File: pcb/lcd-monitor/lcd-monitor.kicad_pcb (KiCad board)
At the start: 2 copper layers, 50 parts, among them J1 Conn_01x07_Male, J2 Conn_01x08_Male, J3 Conn_02x05_Odd_Even, J4 Screw_Terminal_01x02, J5 Conn_01x06_Male, SW1 SW_Push, U1 PC817, U10 AZ1117-3.3, U2 PC817, U3 PC817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

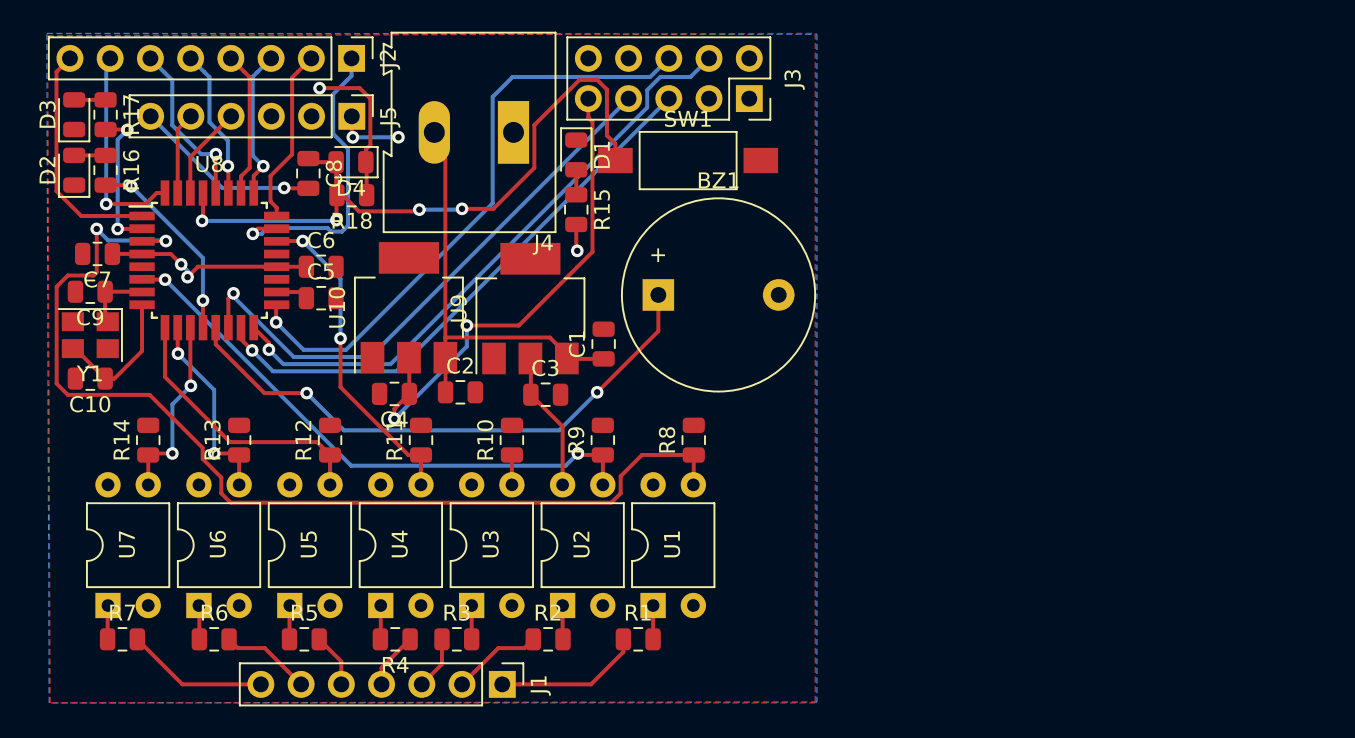
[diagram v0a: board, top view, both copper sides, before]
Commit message: Add zone status led
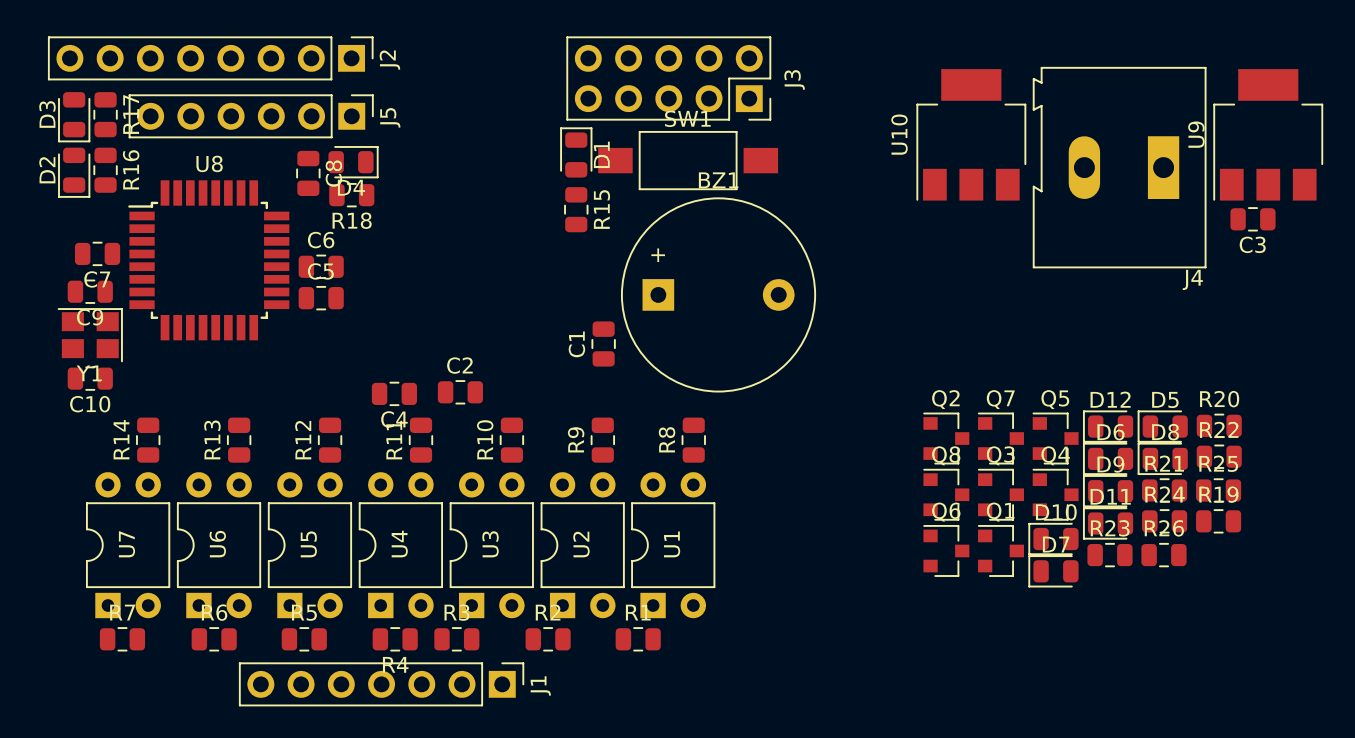
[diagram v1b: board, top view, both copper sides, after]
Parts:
- added D10: LED, LED_SMD:LED_0805_2012Metric, F.Cu at (205.2, 85.7)
- added D11: LED, LED_SMD:LED_0805_2012Metric, F.Cu at (208.7, 84.7)
- added D12: D, Diode_SMD:D_0805_2012Metric, F.Cu at (208.7, 78.6)
- added D5: LED, LED_SMD:LED_0805_2012Metric, F.Cu at (212.1, 78.6)
- added D6: LED, LED_SMD:LED_0805_2012Metric, F.Cu at (208.7, 80.7)
- added D7: LED, LED_SMD:LED_0805_2012Metric, F.Cu at (205.2, 87.8)
- added D8: LED, LED_SMD:LED_0805_2012Metric, F.Cu at (212.1, 80.7)
- added D9: LED, LED_SMD:LED_0805_2012Metric, F.Cu at (208.7, 82.7)
- added Q1: 2N7002, Package_TO_SOT_SMD:SOT-23, F.Cu at (201.8, 86.5)
- added Q2: 2N7002, Package_TO_SOT_SMD:SOT-23, F.Cu at (198.3, 79.4)
- added Q3: 2N7002, Package_TO_SOT_SMD:SOT-23, F.Cu at (201.8, 82.9)
- added Q4: 2N7002, Package_TO_SOT_SMD:SOT-23, F.Cu at (205.2, 82.9)
- added Q5: 2N7002, Package_TO_SOT_SMD:SOT-23, F.Cu at (205.2, 79.4)
- added Q6: 2N7002, Package_TO_SOT_SMD:SOT-23, F.Cu at (198.3, 86.5)
- added Q7: 2N7002, Package_TO_SOT_SMD:SOT-23, F.Cu at (201.8, 79.4)
- added Q8: 2N7002, Package_TO_SOT_SMD:SOT-23, F.Cu at (198.3, 82.9)
- added R19: 10K, Resistor_SMD:R_0805_2012Metric, F.Cu at (215.5, 84.6)
- added R20: 10K, Resistor_SMD:R_0805_2012Metric, F.Cu at (215.6, 78.6)
- added R21: 10K, Resistor_SMD:R_0805_2012Metric, F.Cu at (212.1, 82.7)
- added R22: 10K, Resistor_SMD:R_0805_2012Metric, F.Cu at (215.6, 80.5)
- added R23: 10K, Resistor_SMD:R_0805_2012Metric, F.Cu at (208.7, 86.7)
- added R24: 10K, Resistor_SMD:R_0805_2012Metric, F.Cu at (212.1, 84.6)
- added R25: 10K, Resistor_SMD:R_0805_2012Metric, F.Cu at (215.5, 82.7)
- added R26: 100K, Resistor_SMD:R_0805_2012Metric, F.Cu at (212.1, 86.7)
- D4: value D -> LED; footprint Diode_SMD:D_0805_2012Metric -> LED_SMD:LED_0805_2012Metric
- R18: value 100k -> 10K
- moved U9 47.9 mm to (218.6, 60.2)
- moved C3 46.0 mm to (217.7, 65.5), turned to 180 degrees
- moved J4 41.1 mm to (212.0, 62.3)
- moved U10 37.2 mm to (199.9, 60.2)
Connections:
- D4 pad 1: +5V -> GND
- D4 pad 2: Reset -> Net-(D4-Pad2)
- R18 pad 1: +5V -> Net-(D4-Pad2)
- R18 pad 2: Reset -> +5V
- Y1 pad 2: (no net) -> Crystal_B
- Y1 pad 3: Crystal_B -> (no net)
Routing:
- net S1: track 66.1 -> 0.00 mm, vias 2 -> 0
- net Reset: track 45.2 -> 0.00 mm, vias 4 -> 0
- net MISO: track 38.6 -> 0.00 mm, vias 1 -> 0
- net SCK: track 38.2 -> 0.00 mm, vias 1 -> 0
- net +5V: track 36.8 -> 0.00 mm, vias 4 -> 0
- net S2: track 36.2 -> 0.00 mm, vias 2 -> 0
- net Buzzer: track 36.1 -> 0.00 mm, vias 2 -> 0
- net CS: track 35.8 -> 0.00 mm, vias 1 -> 0
- net MOSI: track 35.7 -> 0.00 mm, vias 1 -> 0
- net +3V3: track 31.8 -> 0.00 mm, vias 2 -> 0
- net +12V: track 27.4 -> 0.00 mm
- net S4: track 20.6 -> 0.00 mm, vias 2 -> 0
- net Key_1: track 19.5 -> 0.00 mm, vias 1 -> 0
- net S5: track 17.5 -> 0.00 mm
- net Key_8: track 14.8 -> 0.00 mm
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- removed copper zone on B.Cu, net +5V
- removed copper zone on F.Cu, net GND
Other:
- net class power added: clearance 0.2, trace_width 0.25, via_dia 0.8, via_drill 0.4
- rule via_min_size: 0 -> 0.6
